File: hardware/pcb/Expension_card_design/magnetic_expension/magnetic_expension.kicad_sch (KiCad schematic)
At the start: 6 parts, among them J1 528850274

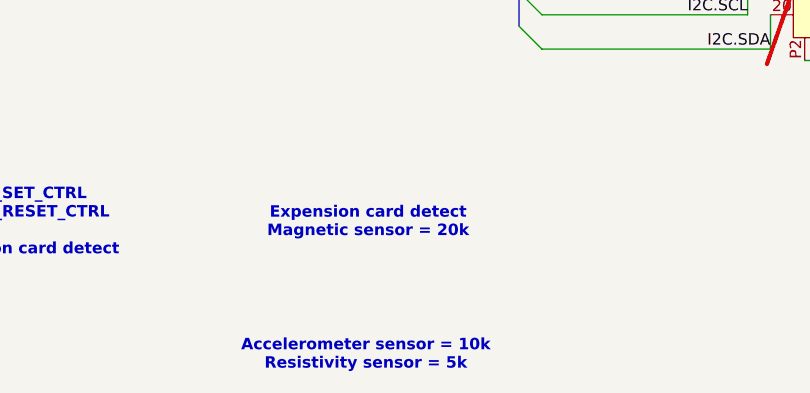
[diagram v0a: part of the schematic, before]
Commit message: Backup avant deletion offset/dac
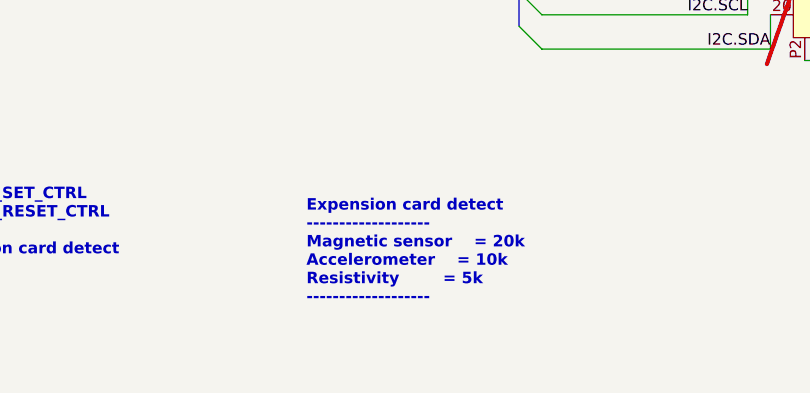
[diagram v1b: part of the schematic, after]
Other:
- note added: "Expension card detect ------------------- Magnetic sensor = 20k Accelerometer = 10k Resistivity = 5k -------------------"
- note removed: "Accelerometer sensor = 10k Resistivity sensor = 5k"
- note removed: "Expension card detect Magnetic sensor = 20k"
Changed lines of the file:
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@@
 		)
 	)
-	(text "Expension card detect\nMagnetic sensor = 20k"
+	(text "Expension card detect\n-------------------\nMagnetic sensor	= 20k\nAccelerometer	= 10k\nResistivity		= 5k\n-------------------"
 		(exclude_from_sim no)
-		(at 94.996 153.924 0)
+		(at 88.138 157.226 0)
 		(effects
 			(font
@@
 				(bold yes)
 			)
+			(justify left)
 		)
 	)
-	(text "Accelerometer sensor = 10k\nResistivity sensor = 5k"
-		(exclude_from_sim no)
-		(at 94.742 168.656 0)
-		(effects
-			(font
-				(size 1.27 1.27)
-				(thickness 0.254)
-				(bold yes)
-			)
-		)
-	)

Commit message: ADC_Fixed
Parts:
- J1: now fitted
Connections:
- net +18V: now also J1.12; no longer J1.13
- net +1V65: now also J1.11; no longer J1.12
- net +5VA: now also J1.13; no longer J1.14
- net +9VA: now also J1.15; no longer J1.16
- net -5VA: now also J1.14; no longer J1.15
- net GND: no longer J1.11
- net SENSOR_RESET_CTRL: now also J1.17; no longer J1.18
- net SENSOR_SET_CTRL: now also J1.16; no longer J1.17
- new net +3V3D: J1.18

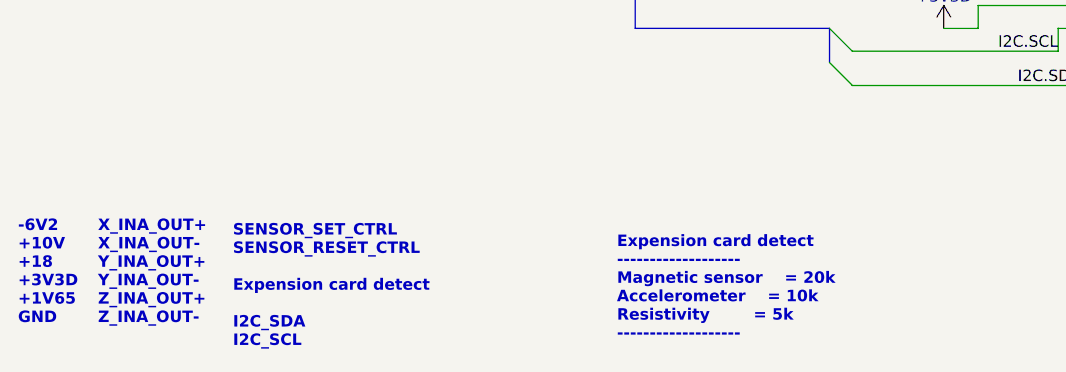
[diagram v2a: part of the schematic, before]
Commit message: calibration on the z and x axis
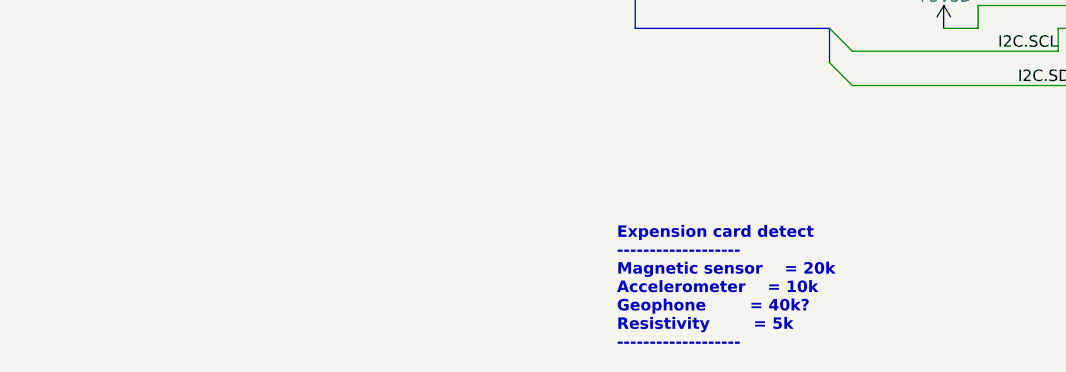
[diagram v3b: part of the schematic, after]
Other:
- note added: "Expension card detect ------------------- Magnetic sensor = 20k Accelerometer = 10k Geophone = 40k? Resistivity = 5k -------------------"
- note removed: "-6V2 +10V +18 +3V3D +1V65 GND"
- note removed: "Expension card detect ------------------- Magnetic sensor = 20k Accelerometer = 10k Resistivity = 5k -------------------"
- note removed: "SENSOR_SET_CTRL SENSOR_RESET_CTRL Expension card detect I2C_SDA I2C_SCL"
- note removed: "X_INA_OUT+ X_INA_OUT- Y_INA_OUT+ Y_INA_OUT- Z_INA_OUT+ Z_INA_OUT-"
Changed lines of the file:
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@@
 		(members "CLK" "CMD" "D0" "D1" "D2" "D3")
 	)
-	(text "SENSOR_SET_CTRL\nSENSOR_RESET_CTRL\n\nExpension card detect\n\nI2C_SDA\nI2C_SCL"
-		(exclude_from_sim no)
-		(at 45.466 156.972 0)
-		(effects
-			(font
-				(size 1.27 1.27)
-				(thickness 0.254)
-				(bold yes)
-			)
-			(justify left)
-		)
-	)
-	(text "Expension card detect\n-------------------\nMagnetic sensor	= 20k\nAccelerometer	= 10k\nResistivity		= 5k\n-------------------"
+	(text "Expension card detect\n-------------------\nMagnetic sensor	= 20k\nAccelerometer	= 10k\nGeophone		= 40k?\nResistivity		= 5k\n-------------------"
 		(exclude_from_sim no)
 		(at 88.138 157.226 0)
-		(effects
-			(font
-				(size 1.27 1.27)
-				(thickness 0.254)
-				(bold yes)
-			)
-			(justify left)
-		)
-	)
-	(text "X_INA_OUT+\nX_INA_OUT-\nY_INA_OUT+\nY_INA_OUT-\nZ_INA_OUT+\nZ_INA_OUT-"
-		(exclude_from_sim no)
-		(at 30.48 155.448 0)
-		(effects
-			(font
-				(size 1.27 1.27)
-				(thickness 0.254)
-				(bold yes)
-			)
-			(justify left)
-		)
-	)
-	(text "-6V2\n+10V\n+18\n+3V3D\n+1V65\nGND"
-		(exclude_from_sim no)
-		(at 21.59 155.448 0)
 		(effects
 			(font
@@
 			)
 		)
-		(property "Sim.Enable" ""
-			(at 39.37 82.55 0)
-			(effects
-				(font
-					(size 1.27 1.27)
-				)
-				(hide yes)
-			)
-		)
 		(instances
 			(project ""
@@
 			)
 		)
-		(property "Sim.Enable" ""
-			(at 39.37 87.63 0)
-			(effects
-				(font
-					(size 1.27 1.27)
-				)
-				(hide yes)
-			)
-		)
 		(instances
 			(project "magnetic_expension"
@@
 		)
 		(property "LCSC" "C4184"
-			(at 166.37 104.14 0)
-			(effects
-				(font
-					(size 1.27 1.27)
-				)
-				(hide yes)
-			)
-		)
-		(property "Sim.Enable" ""
 			(at 166.37 104.14 0)
 			(effects
@@
 			)
 		)
-		(property "Sim.Enable" ""
-			(at 144.78 119.38 0)
-			(effects
-				(font
-					(size 1.27 1.27)
-				)
-				(hide yes)
-			)
-		)
 		(pin "10"
 		)
@@
 			)
 		)
-		(property "Sim.Enable" ""
-			(at 39.37 97.79 90)
-			(effects
-				(font
-					(size 1.27 1.27)
-				)
-				(hide yes)
-			)
-		)
 		(instances
 			(project "magnetic_expension"
@@
 			(at 39.37 92.71 0)
 			(effects
-				(font
-					(size 1.27 1.27)
-				)
-				(hide yes)
-			)
-		)
-		(property "Sim.Enable" ""
-			(at 39.37 92.71 0)
-			(effects

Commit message: Work in progress rev2
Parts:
- removed H1, H2, H3, H4: MountingHole, MountingHole:MountingHole_4.3mm_M4, symbol Mechanical:MountingHole
- removed J1: 528850274, magnode_footprints:CON_528850274_MOL, symbol magnode_symbols:528850274
- removed R1: 20k, Resistor_SMD:R_0603_1608Metric, symbol Device:R
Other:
- added sheet CONNECTOR (schematics/CONN.kicad_sch)
- sheet SENSOR_OFFSET_DRIVERS ports: added I2C{SDA SCL}; removed I2C{SDA, SDO, SCL}

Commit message: ...
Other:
- sheet ANALOG_FRONTEND_INA851 renamed INA_GAIN
- sheet SENSOR_OFFSET_DRIVERS renamed MAGNETIC_OFFSET_DRIVERS
- added sheet BRIDGE_DC_OFFSET (schematics/Bridge_offset.kicad_sch)

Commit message: clearing git
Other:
- sheet BRIDGE_DC_OFFSET renamed BRIDGE_OFFSET
- sheet BRIDGE_OFFSET ports: added X_INA_OUT_F+, X_INA_OUT_F-, Y_INA_OUT_F+, Y_INA_OUT_F-, Z_INA_OUT_F+, Z_INA_OUT_F-; removed X_INA_OUT+, X_INA_OUT-, Y_INA_OUT+, Y_INA_OUT-, Z_INA_OUT+, Z_INA_OUT-
- sheet CONNECTOR ports: added X_CONN+, X_CONN-, Y_CONN+, Y_CONN-, Z_CONN+, Z_CONN-; removed X_INA_OUT+, X_INA_OUT-, Y_INA_OUT+, Y_INA_OUT-, Z_INA_OUT+, Z_INA_OUT-
- sheet INA_GAIN ports: added X_INA_OUT_F+, X_INA_OUT_F-, Y_INA_OUT_F+, Y_INA_OUT_F-, Z_INA_OUT_F+, Z_INA_OUT_F-; removed X_INA_OUT+, X_INA_OUT-, Y_INA_OUT+, Y_INA_OUT-, Z_INA_OUT+, Z_INA_OUT-
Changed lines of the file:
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@@
 			(color 255 255 194 1.0000)
 		)
-		(property "Sheetname" "BRIDGE_DC_OFFSET"
+		(property "Sheetname" "BRIDGE_OFFSET"
 			(at 215.9 57.3782 0)
 			(effects
@@
 			)
 		)
-		(pin "X_INA_OUT+" input
-			(at 215.9 62.23 180)
-			(effects
-				(font
-					(size 1.27 1.27)
-				)
-				(justify left)
-			)
-		)
-		(pin "X_INA_OUT-" input
-			(at 215.9 64.77 180)
-			(effects
-				(font
-					(size 1.27 1.27)
-				)
-				(justify left)
-			)
-		)
-		(pin "Y_INA_OUT+" input
-			(at 215.9 69.85 180)
-			(effects
-				(font
-					(size 1.27 1.27)
-				)
-				(justify left)
-			)
-		)
-		(pin "Y_INA_OUT-" input
-			(at 215.9 72.39 180)
-			(effects
-				(font
-					(size 1.27 1.27)
-				)
-				(justify left)
-			)
-		)
-		(pin "Z_INA_OUT+" input
-			(at 215.9 77.47 180)
-			(effects
-				(font
-					(size 1.27 1.27)
-				)
-				(justify left)
-			)
-		)
-		(pin "Z_INA_OUT-" input
-			(at 215.9 80.01 180)
-			(effects
-				(font
-					(size 1.27 1.27)
-				)
-				(justify left)
-			)
-		)
 		(pin "X_CONN+" output
 			(at 246.38 62.23 0)
@@
 				)
 				(justify right)
+			)
+		)
+		(pin "X_INA_OUT_F+" input
+			(at 215.9 62.23 180)
+			(effects
+				(font
+					(size 1.27 1.27)
+				)
+				(justify left)
+			)
+		)
+		(pin "X_INA_OUT_F-" input
+			(at 215.9 64.77 180)
+			(effects
+				(font
+					(size 1.27 1.27)
+				)
+				(justify left)
+			)
+		)
+		(pin "Y_INA_OUT_F+" input
+			(at 215.9 69.85 180)
+			(effects
+				(font
+					(size 1.27 1.27)
+				)
+				(justify left)
+			)
+		)
+		(pin "Y_INA_OUT_F-" input
+			(at 215.9 72.39 180)
+			(effects
+				(font
+					(size 1.27 1.27)
+				)
+				(justify left)
+			)
+		)
+		(pin "Z_INA_OUT_F+" input
+			(at 215.9 77.47 180)
+			(effects
+				(font
+					(size 1.27 1.27)
+				)
+				(justify left)
+			)
+		)
+		(pin "Z_INA_OUT_F-" input
+			(at 215.9 80.01 180)
+			(effects
+				(font
+					(size 1.27 1.27)
+				)
+				(justify left)
 			)
 		)
@@
 			)
 		)
-		(pin "X_INA_OUT+" input
+		(pin "X_CONN+" output
 			(at 179.07 133.35 0)
 			(effects
@@
 			)
 		)
-		(pin "X_INA_OUT-" input
+		(pin "X_CONN-" output
 			(at 179.07 130.81 0)
 			(effects
@@
 			)
 		)
-		(pin "Y_INA_OUT+" input
+		(pin "Y_CONN+" output
 			(at 179.07 125.73 0)
 			(effects
@@
 			)
 		)
-		(pin "Y_INA_OUT-" input
+		(pin "Y_CONN-" output
 			(at 179.07 123.19 0)
 			(effects
@@
 			)
 		)
-		(pin "Z_INA_OUT+" input
+		(pin "Z_CONN+" output
 			(at 179.07 118.11 0)
 			(effects
@@
 			)
 		)
-		(pin "Z_INA_OUT-" input
+		(pin "Z_CONN-" output
 			(at 179.07 115.57 0)
 			(effects
@@
 			)
 		)
-		(pin "X_INA_OUT+" output
+		(pin "X_INA_OUT_F+" output
 			(at 207.01 62.23 0)
 			(effects
@@
 			)
 		)
-		(pin "X_INA_OUT-" output
+		(pin "X_INA_OUT_F-" output
 			(at 207.01 64.77 0)
 			(effects
@@
 			)
 		)
-		(pin "Y_INA_OUT+" output
+		(pin "Y_INA_OUT_F+" output
 			(at 207.01 69.85 0)
 			(effects
@@
 			)
 		)
-		(pin "Y_INA_OUT-" output
+		(pin "Y_INA_OUT_F-" output
 			(at 207.01 72.39 0)
 			(effects
@@
 			)
 		)
-		(pin "Z_INA_OUT+" output
+		(pin "Z_INA_OUT_F+" output
 			(at 207.01 77.47 0)
 			(effects
@@
 			)
 		)
-		(pin "Z_INA_OUT-" output
+		(pin "Z_INA_OUT_F-" output
 			(at 207.01 80.01 0)
 			(effects
